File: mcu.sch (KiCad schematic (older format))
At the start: 39 parts

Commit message: Finished initial schematic review.
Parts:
- added C? (x7): 100nF, symbol Device:C_Small
- added C? (x3): 2.2uF, symbol Device:C_Small
- added C?: 4.7uF, symbol Device:C_Small
- added C?: 10nF, symbol Device:C_Small
- added R?: 47k, symbol Device:R
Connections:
- net labels added: I2S_MCK, JTCK, JTDI, JTDO, JTMS, JTRST, SPI0_CS0, SPI0_CS1, SPI0_MISO, SPI0_MOSI, SPI0_SCK, SPI1_CS0, SPI1_CS1, SPI1_MISO, SPI1_MOSI, SPI1_SCK
- net labels removed: SPI_CS, SPI_MISO, SPI_MOSI, SPI_SCK, UART1_RX, UART1_TX
- wire segments 241 -> 301
- no-connect marks 12 -> 48

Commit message: Tweak I2S breakout, generate netlist.
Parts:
- removed C?: 10nF, symbol Device:C_Small
- removed C?: 2.2uF, symbol Device:C_Small
- C15, C16, C17, C18, C19, C20, C21, C22, C23, C24, C26, C28, C29, C30, C31, C32, C33, C34, C35, C36, C37, C38: renamed from C?; footprint (none) -> Capacitor_SMD:C_0603_1608Metric
- J11, J12: renamed from J?; footprint (none) -> Connector_RJ:RJ45_Amphenol_RJHSE5380
- J13: renamed from J?; footprint HR911105A_1 -> SamacSys_Parts:HR911105A_1
- L1: renamed from L?; footprint (none) -> Inductor_SMD:L_0603_1608Metric
- R19, R20, R21, R22, R23, R24, R25, R26, R27, R28, R29, R30, R31, R32, R33, R34, R35, R36, R37, R38: renamed from R?; footprint (none) -> Resistor_SMD:R_0603_1608Metric
- U4: renamed from U?; footprint Package_DIP:DIP-8_W7.62mm -> Package_DIP:DIP-8_W7.62mm_Socket
- Y1: renamed from Y?; footprint (none) -> Crystal:Crystal_SMD_Abracon_ABM8G-4Pin_3.2x2.5mm
- gave numbers to parts that had none: 2
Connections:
- net labels added: I2S_WS, MCU_VDDA
- wire segments 301 -> 299
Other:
- note added: "Xtal: ABM8-25.000MHZ-10-D1G-T"

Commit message: Sorted passives on board.
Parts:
- J13: symbol SamacSys_Parts:HR911105A -> panel_light_control-rescue:HR911105A-SamacSys_Parts
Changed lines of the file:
@@
 $EndDescr
 $Comp
-L SamacSys_Parts:HR911105A J13
+L panel_light_control-rescue:HR911105A-SamacSys_Parts J13
 U 1 1 5BBC51BA
 P 9650 5350

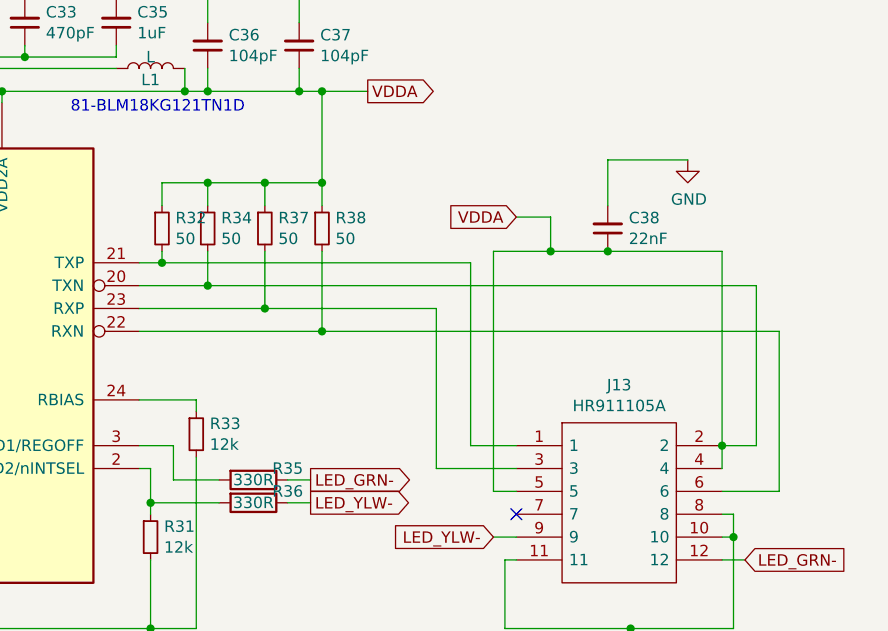
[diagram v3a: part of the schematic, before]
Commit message: Finished basic board layout.
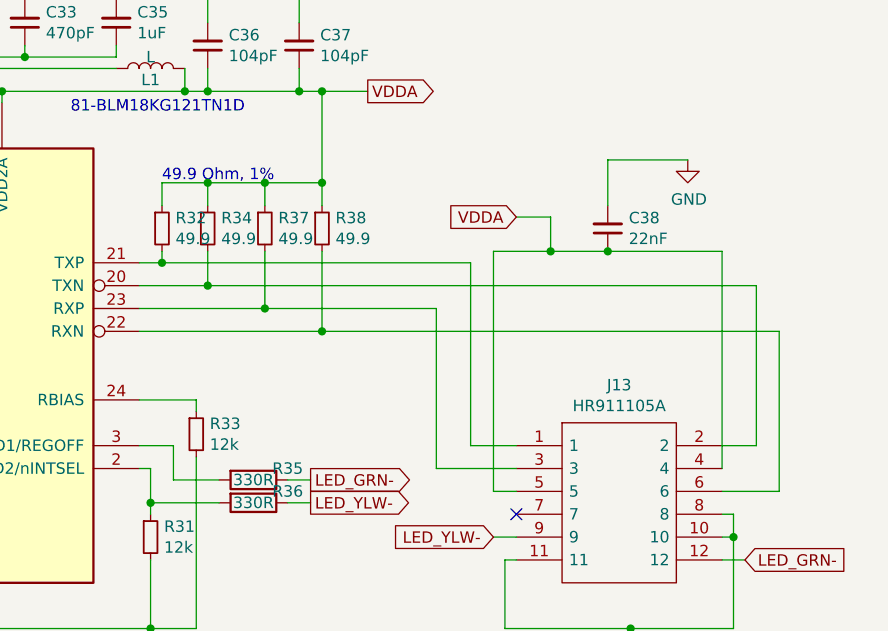
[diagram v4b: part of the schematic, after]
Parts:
- R32, R34, R37, R38: value 50 -> 49.9
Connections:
- net VDDA: no longer J13.2, R34.2, U5.20 (TXN)
- new net: J13.2, R34.2, U5.20 (TXN)
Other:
- note added: "49.9 Ohm, 1%"
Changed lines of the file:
@@
 P 8100 4400
 F 0 "R32" H 8159 4446 50  0000 L CNN
-F 1 "50" H 8159 4355 50  0000 L CNN
+F 1 "49.9" H 8159 4355 50  0000 L CNN
 F 2 "Resistor_SMD:R_0603_1608Metric" H 8100 4400 50  0001 C CNN
 F 3 "~" H 8100 4400 50  0001 C CNN
@@
 P 8300 4400
 F 0 "R34" H 8359 4446 50  0000 L CNN
-F 1 "50" H 8359 4355 50  0000 L CNN
+F 1 "49.9" H 8359 4355 50  0000 L CNN
 F 2 "Resistor_SMD:R_0603_1608Metric" H 8300 4400 50  0001 C CNN
 F 3 "~" H 8300 4400 50  0001 C CNN
@@
 P 8550 4400
 F 0 "R37" H 8609 4446 50  0000 L CNN
-F 1 "50" H 8609 4355 50  0000 L CNN
+F 1 "49.9" H 8609 4355 50  0000 L CNN
 F 2 "Resistor_SMD:R_0603_1608Metric" H 8550 4400 50  0001 C CNN
 F 3 "~" H 8550 4400 50  0001 C CNN
@@
 P 8800 4400
 F 0 "R38" H 8859 4446 50  0000 L CNN
-F 1 "50" H 8859 4355 50  0000 L CNN
+F 1 "49.9" H 8859 4355 50  0000 L CNN
 F 2 "Resistor_SMD:R_0603_1608Metric" H 8800 4400 50  0001 C CNN
 F 3 "~" H 8800 4400 50  0001 C CNN
@@
 	9550 4500 9800 4500
 Wire Wire Line
-	10550 5450 10550 5350
-Wire Wire Line
 	10550 4500 10050 4500
-Connection ~ 10550 5350
-Wire Wire Line
-	10550 5350 10550 4500
 Connection ~ 10050 4500
 $Comp
@@
 Wire Wire Line
 	1600 6200 1500 6200
+Wire Wire Line
+	10550 4500 10550 5450
+Text Notes 8100 4200 0    50   ~ 0
+49.9 Ohm, 1%
 $EndSCHEMATC

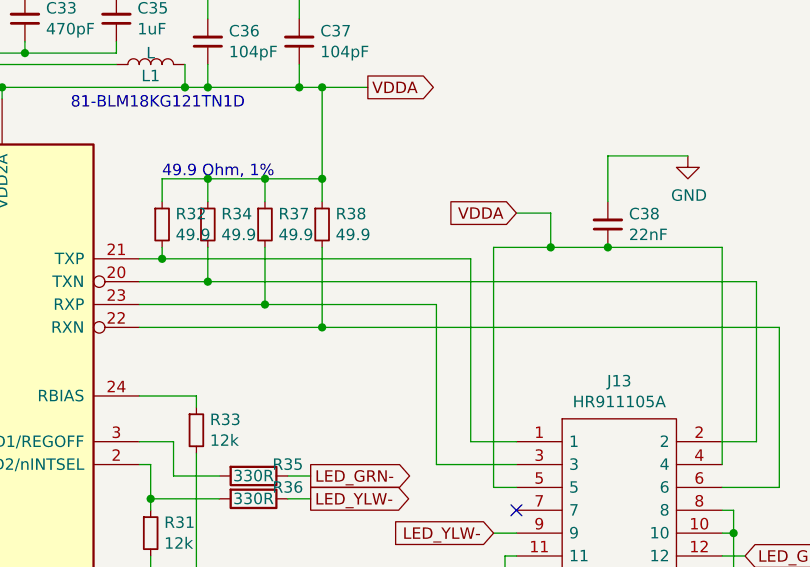
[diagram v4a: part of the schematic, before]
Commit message: Finished initial PHY-magjack routing.
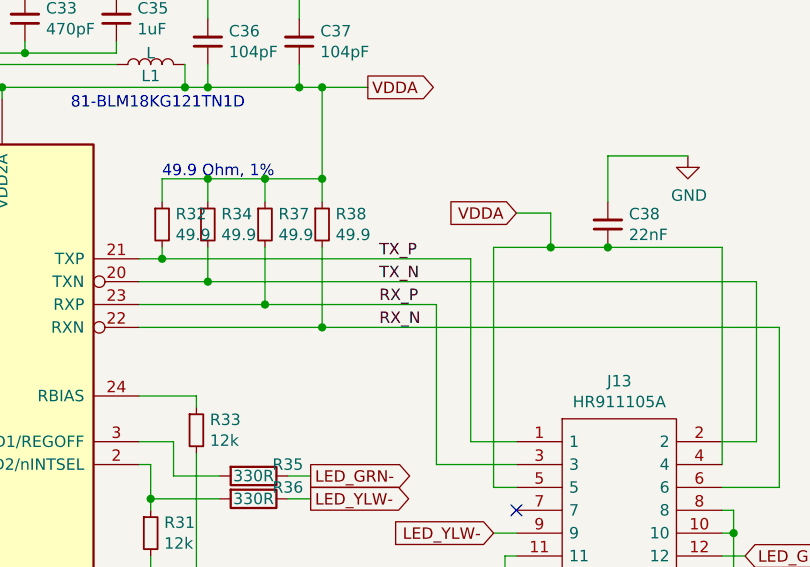
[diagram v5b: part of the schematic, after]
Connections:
- net TX_P: now reaches J13.1, R32.2, U5.21 (TXP)
- net TX_N: now reaches J13.2, R34.2, U5.20 (TXN)
- net RX_P: now reaches J13.3, R37.2, U5.23 (RXP)
- net RX_N: now reaches J13.6, R38.2, U5.22 (RXN)
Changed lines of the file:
@@
 Text Notes 8100 4200 0    50   ~ 0
 49.9 Ohm, 1%
+Text Label 9050 4550 0    50   ~ 0
+TX_P
+Text Label 9050 4650 0    50   ~ 0
+TX_N
+Text Label 9050 4750 0    50   ~ 0
+RX_P
+Text Label 9050 4850 0    50   ~ 0
+RX_N
 $EndSCHEMATC

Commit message: adds PHY PU/PD config pin comments
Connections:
- net LED_GRN-: now also J13.9; no longer J13.12
- net LED_YLW-: now also J13.12; no longer J13.9
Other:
- note added: "(PD):PHYAD0=0"
- note added: "(PU):MODE0"
- note added: "(PU):MODE1"
- note added: "(PU):MODE2"
- note added: "GN.A"
- note added: "MDIO:PU(802.3)"
- note added: "MODE:111 \n= all capable"
- note added: "PD: REF_CLK"
- note added: "PD:REG ON"
- note added: "Y.A"
- note added: "prescribed 12k"
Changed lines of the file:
@@
 	1    0    0    -1
 $EndComp
-Text GLabel 9550 5750 0    50   Input ~ 0
+Text GLabel 10650 5850 2    50   Input ~ 0
 LED_YLW-
 Wire Wire Line
@@
 U 1 1 5BC5BEB3
 P 6200 4750
-F 0 "R22" V 6150 4900 50  0000 C CNN
+F 0 "R22" V 6150 4950 50  0000 C CNN
 F 1 "10R" V 6200 4750 50  0000 C CNN
 F 2 "Resistor_SMD:R_0603_1608Metric" V 6130 4750 50  0001 C CNN
@@
 U 1 1 5BC5BEED
 P 6200 4850
-F 0 "R23" V 6150 5000 50  0000 C CNN
+F 0 "R23" V 6150 5050 50  0000 C CNN
 F 1 "10R" V 6200 4850 50  0000 C CNN
 F 2 "Resistor_SMD:R_0603_1608Metric" V 6130 4850 50  0001 C CNN
@@
 U 1 1 5BC5BFD3
 P 6200 5050
-F 0 "R25" V 6150 5200 50  0000 C CNN
+F 0 "R25" V 6150 5250 50  0000 C CNN
 F 1 "10R" V 6200 5050 50  0000 C CNN
 F 2 "Resistor_SMD:R_0603_1608Metric" V 6130 5050 50  0001 C CNN
@@
 U 1 1 5BC5C00D
 P 6200 4950
-F 0 "R24" V 6150 5100 50  0000 C CNN
+F 0 "R24" V 6150 5150 50  0000 C CNN
 F 1 "10R" V 6200 4950 50  0000 C CNN
 F 2 "Resistor_SMD:R_0603_1608Metric" V 6130 4950 50  0001 C CNN
@@
 Wire Wire Line
 	10600 5650 10600 5750
-Text GLabel 10650 5850 2    50   Input ~ 0
+Text GLabel 9550 5750 0    50   Input ~ 0
 LED_GRN-
 Wire Wire Line
@@
 Text Notes 950  6000 0    50   ~ 0
 MCO1
-Text Notes 4150 5100 0    50   ~ 0
+Text Notes 3850 5050 1    50   ~ 0
 810-C1608C0G2A030C0A or\n603-CC603CRNPO9BN3R0
 Text Notes 7700 3900 0    50   ~ 0
@@
 Wire Wire Line
 	3550 6100 3400 6100
-Text Notes 3800 4850 0    50   ~ 0
+Text Notes 4250 5250 1    50   ~ 0
 Xtal: ABM8-25.000MHZ-10-D1G-T
 Text GLabel 1500 6400 0    50   Input ~ 0
@@
 Text Label 9050 4850 0    50   ~ 0
 RX_N
+Text Notes 7850 5050 0    50   ~ 0
+prescribed 12k
+Text Notes 7350 5300 0    50   ~ 0
+PD:REG ON
+Text Notes 7300 5550 0    50   ~ 0
+PD: REF_CLK
+Text Notes 6350 4400 1    50   ~ 0
+MDIO:PU(802.3)
+Text Notes 4900 4800 0    50   ~ 0
+(PU):MODE0
+Text Notes 4900 4900 0    50   ~ 0
+(PU):MODE1
+Text Notes 4900 5100 0    50   ~ 0
+(PU):MODE2
+Text Notes 4900 5000 0    50   ~ 0
+(PD):PHYAD0=0
+Text Notes 4900 4650 0    50   ~ 0
+MODE:111 \n= all capable
+Text Notes 9950 5800 0    50   ~ 0
+GN.A
+Text Notes 10100 5900 0    50   ~ 0
+Y.A
 $EndSCHEMATC

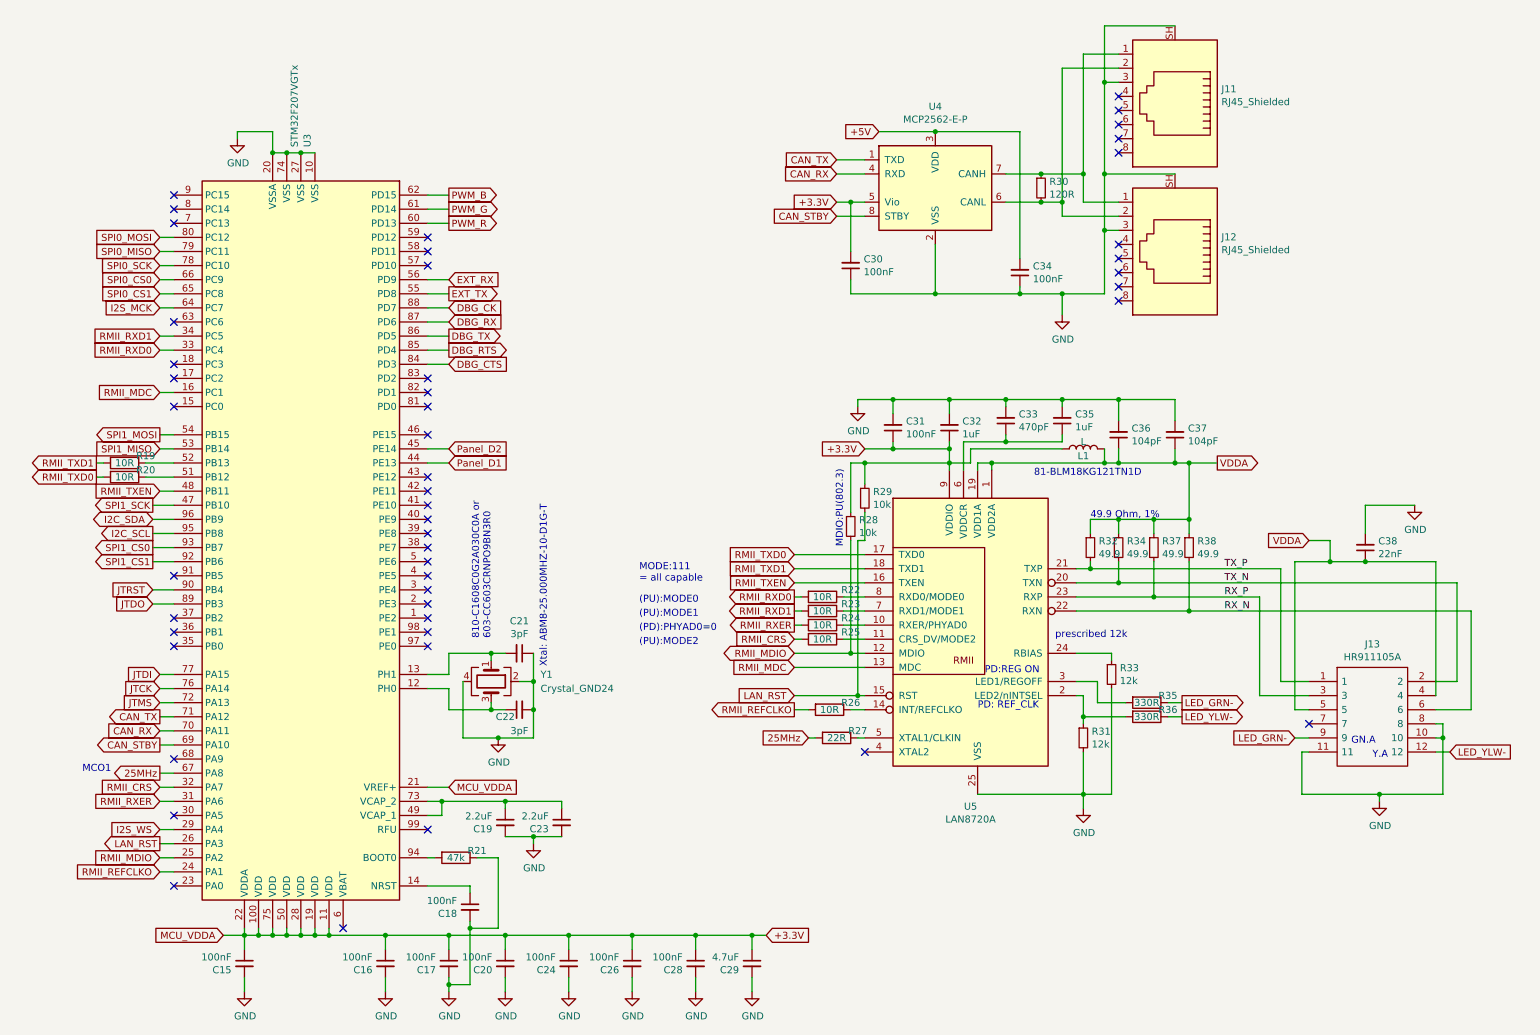
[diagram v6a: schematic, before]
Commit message: schematic clean-up, BOM info partially added
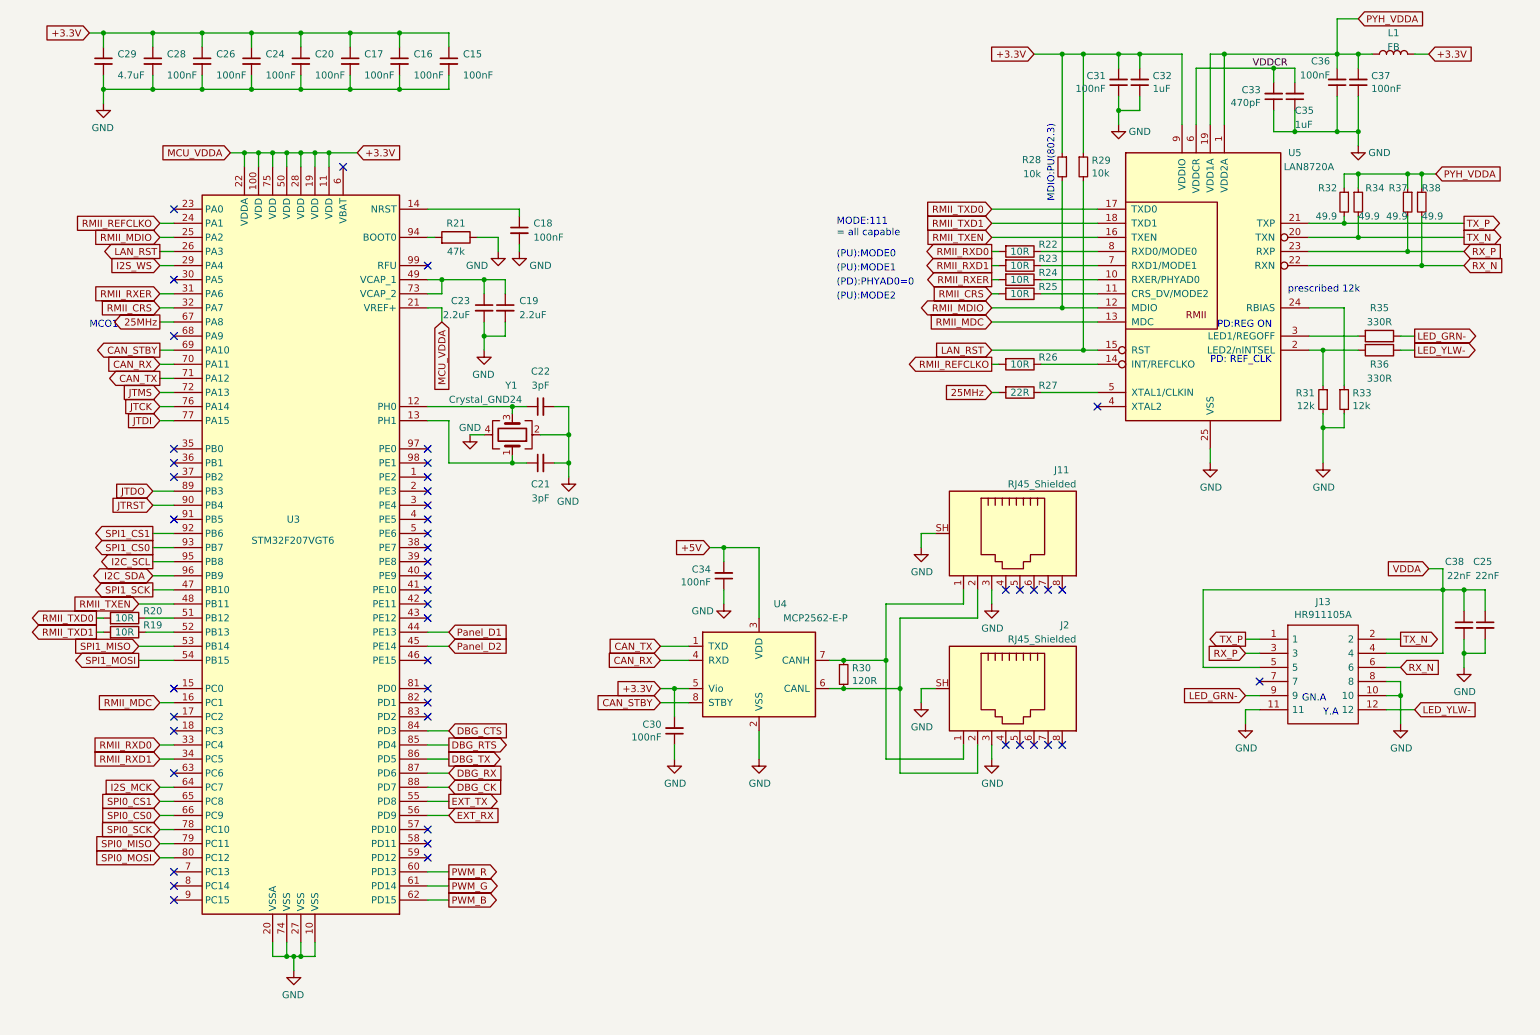
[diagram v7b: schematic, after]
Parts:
- removed J12: RJ45_Shielded, Connector_RJ:RJ45_Amphenol_RJHSE5380, symbol Connector:RJ45_Shielded
- added C25: 22nF, Capacitor_SMD:C_0603_1608Metric, symbol Device:C_Small
- added J2: RJ45_Shielded, Connector_RJ:RJ45_Amphenol_RJHSE5380, symbol Connector:RJ45_Shielded
- C21, C22: MPN (none) -> CC603CRNPO9BN3R0 / C1608C0G2A030C080AA; Mouser (none) -> 603-CC603CRNPO9BN3R0 / 810-C1608C0G2A030C0A
- C36, C37: value 104pF -> 100nF
- J11: MPN (none) -> RJHSE-5380; Mouser (none) -> 523-RJHSE-5380
- J13: AliExpress (none) -> HR911105A; Mouser (none) -> 710-7499011121A (WE equivalent)
- L1: value L -> FB; MPN (none) -> BLM18KG121TN1D; Mouser (none) -> 81-BLM18KG121TN1D
- U3: value STM32F207VGTx -> STM32F207VGT6; MPN (none) -> STM32F207VGT6; Mouser (none) -> 511-STM32F207VGT6
- U4: MPN (none) -> MCP2562-E/P; Mouser (none) -> 579-MCP2562-E/P
- U5: MPN (none) -> LAN8720A-CP-TR-ABC; Mouser (none) -> 579-LAN8720ACPTRABC
- Y1: MPN (none) -> ABM8-25.000MHZ-10-D1G-T; Mouser (none) -> 815-ABM8-25-10-D1G-T
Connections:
- net +3.3V: now also C31.2, C32.2, L1.2; no longer C31.1, C32.1, L1.1
- net GND: now also C21.2, C31.1, C32.1, C33.1, C35.1, C36.1, C37.1, C25.2, J2.3, J2.SH; no longer C21.1, C31.2, C32.2, C33.2, C35.2, C36.2, C37.2
- net VDDA: now also C25.1; no longer C36.1, C37.1, L1.2, R32.1, R34.1, R37.1, R38.1, U5.1 (VDD2A), U5.19 (VDD1A)
- net at U3.13 (PH1), Y1.1: now also C21.1; no longer C21.2
- net at J11.2, R30.2, U4.6 (CANL): now also J2.2
- net at J11.1, R30.1, U4.7 (CANH): now also J2.1
- new net PYH_VDDA: C36.2, C37.2, L1.1, R32.1, R34.1, R37.1, R38.1, U5.1 (VDD2A), U5.19 (VDD1A)
- new net VDDCR: C33.2, C35.2, U5.6 (VDDCR)
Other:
- note removed: "49.9 Ohm, 1%"
- note removed: "81-BLM18KG121TN1D"
- note removed: "810-C1608C0G2A030C0A or\n603-CC603CRNPO9BN3R0"
- note removed: "Xtal: ABM8-25.000MHZ-10-D1G-T"
- moved on the sheet: C15, C16, C17, C18, C19, C20, C22, C23, C24, C26, C28, C29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
